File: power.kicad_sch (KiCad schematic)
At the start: 41 parts, among them U19 AP62301_TSOT, U20 AP62301_TSOT, U24 AP62301_TSOT, U38 TPS22976DPUR, U42 TPS22976DPUR

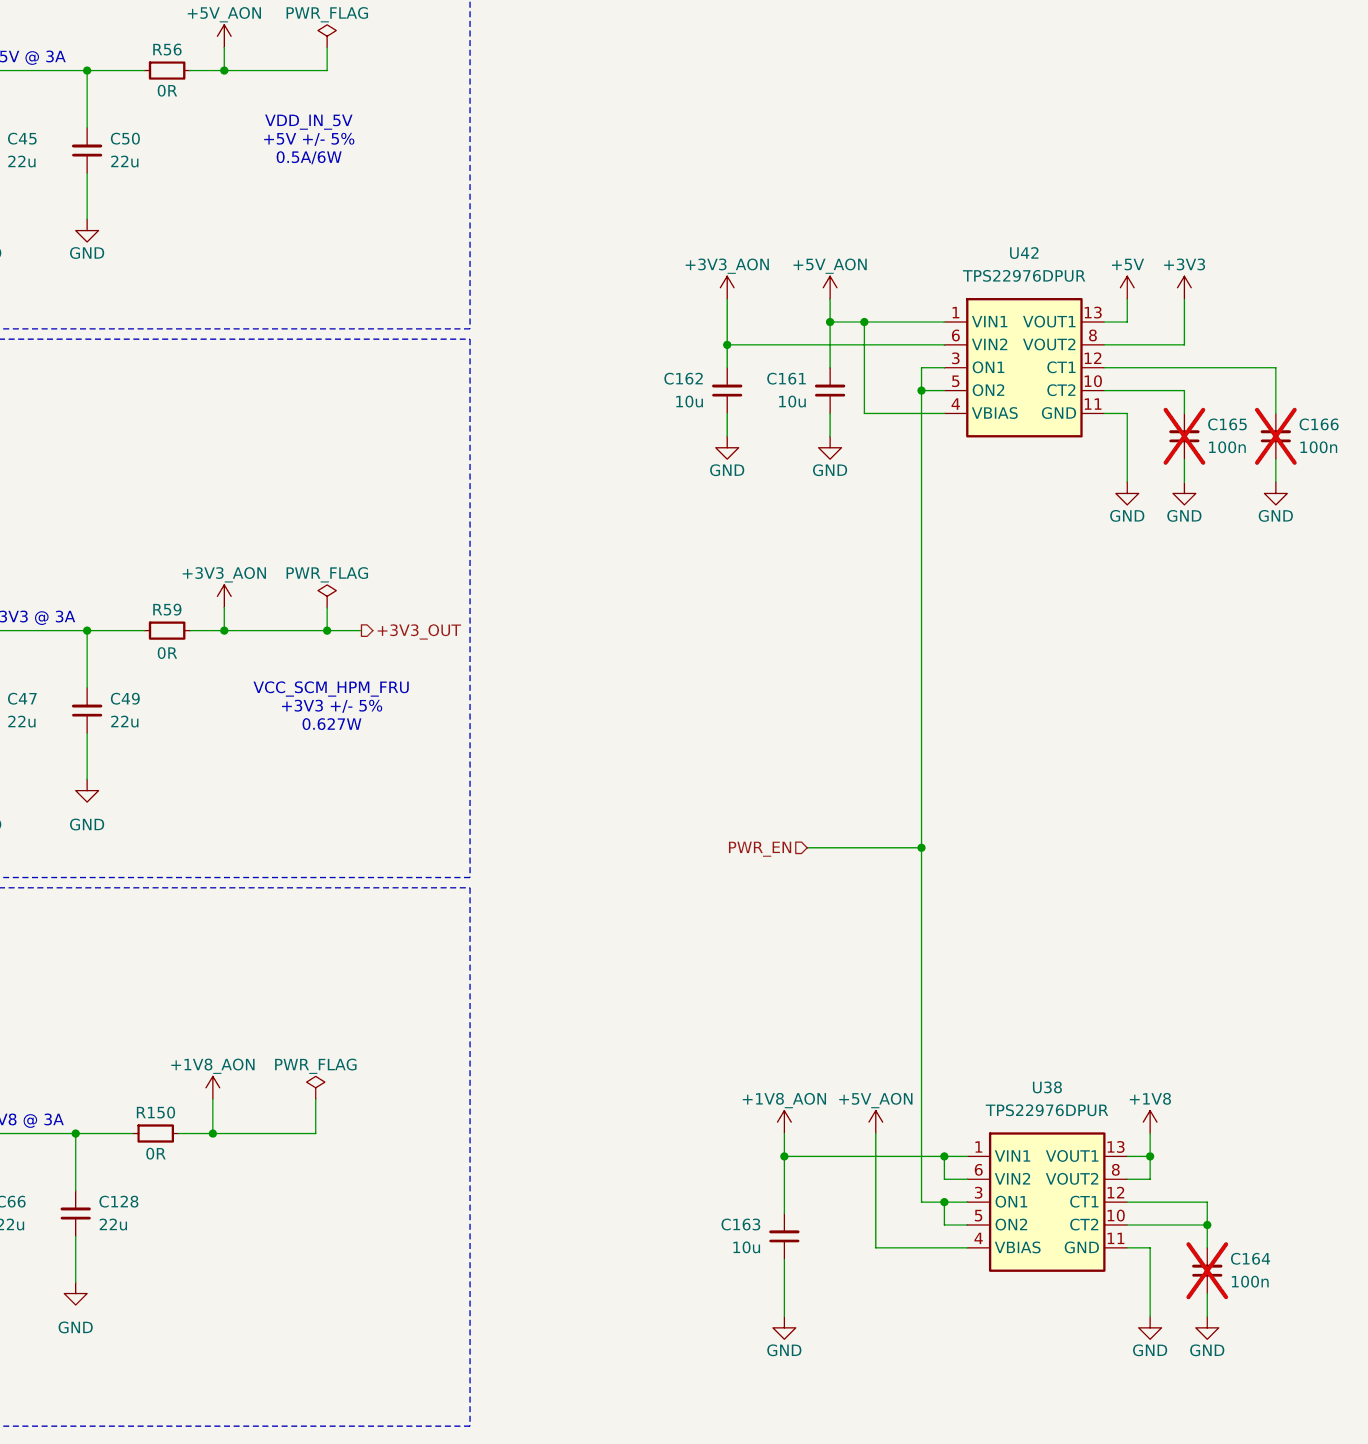
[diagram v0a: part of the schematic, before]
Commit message: [#83609] Connect PWR_EN signal, change eMMC power to AON, minor schematic refactor
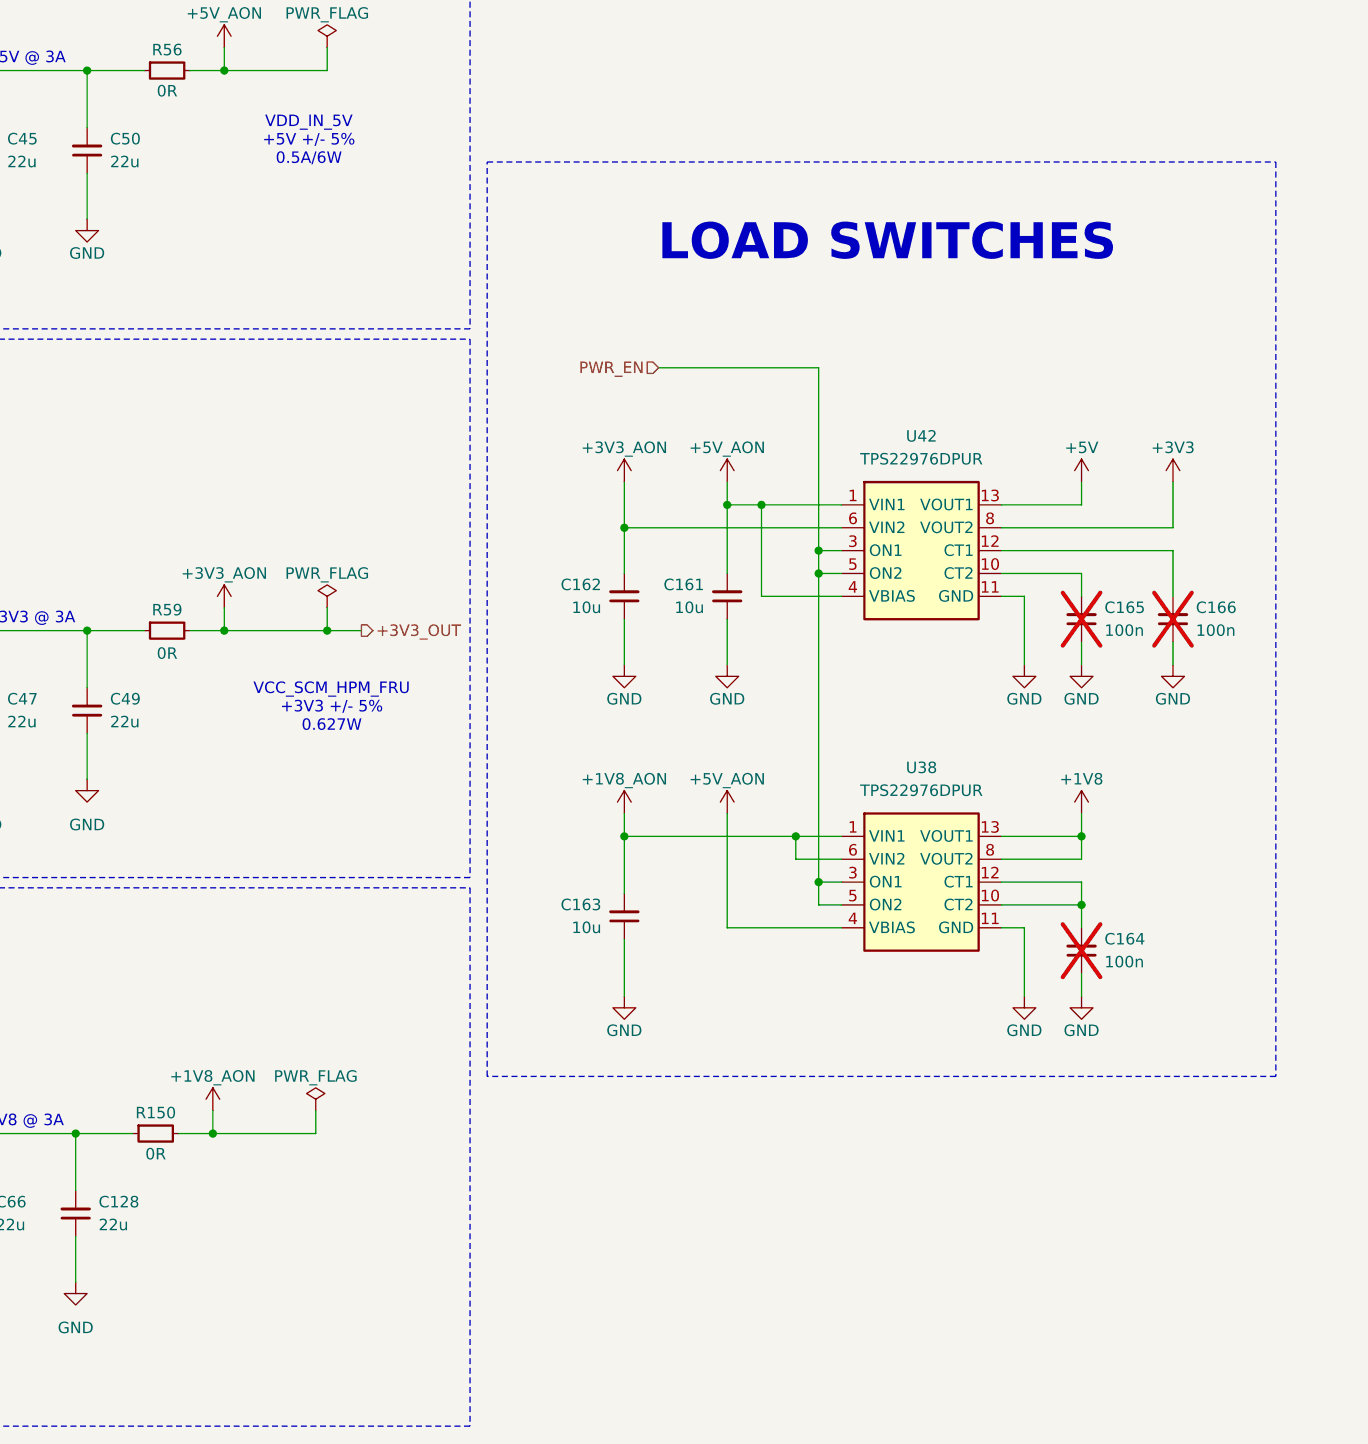
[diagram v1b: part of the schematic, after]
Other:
- note added: "LOAD SWITCHES"
- moved on the sheet: C161, C162, C163, C164, C165, C166, U38, U42

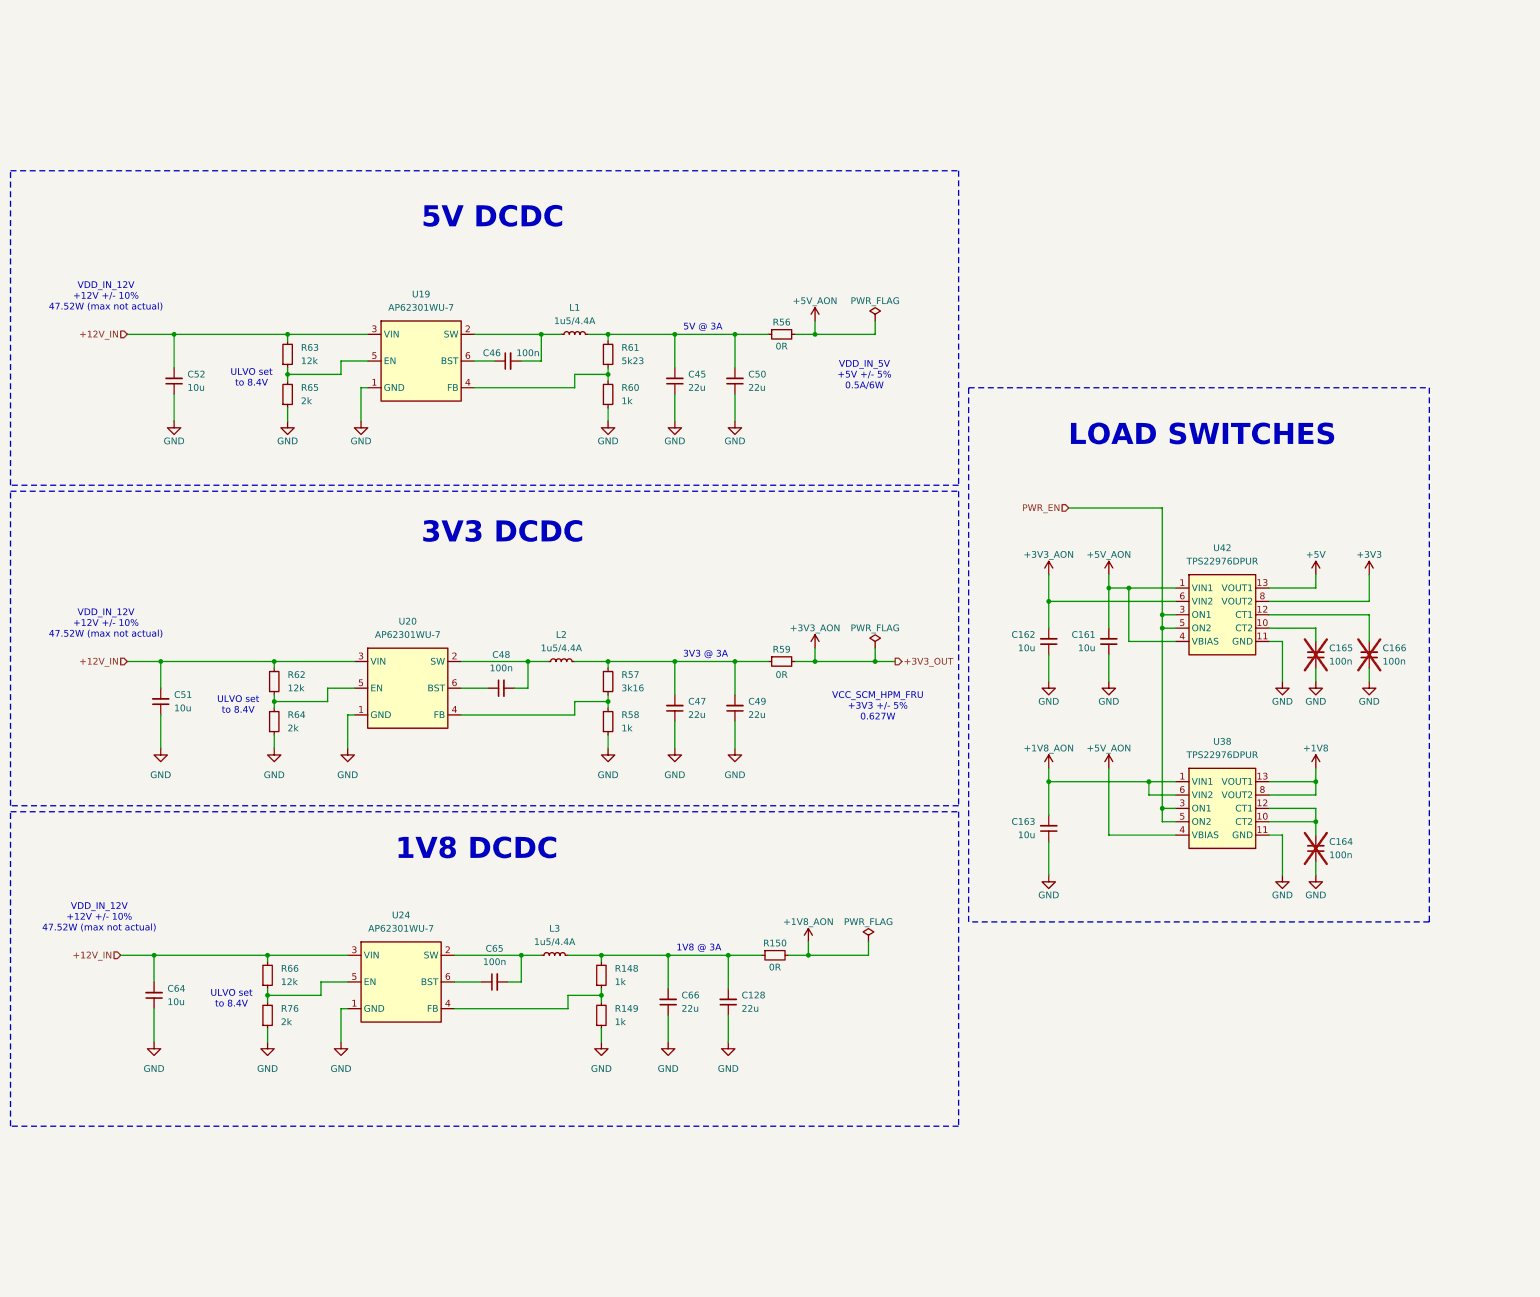
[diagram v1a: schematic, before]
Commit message: [#83609] Move +5V to double switch. Add indicator LEDs and TPs
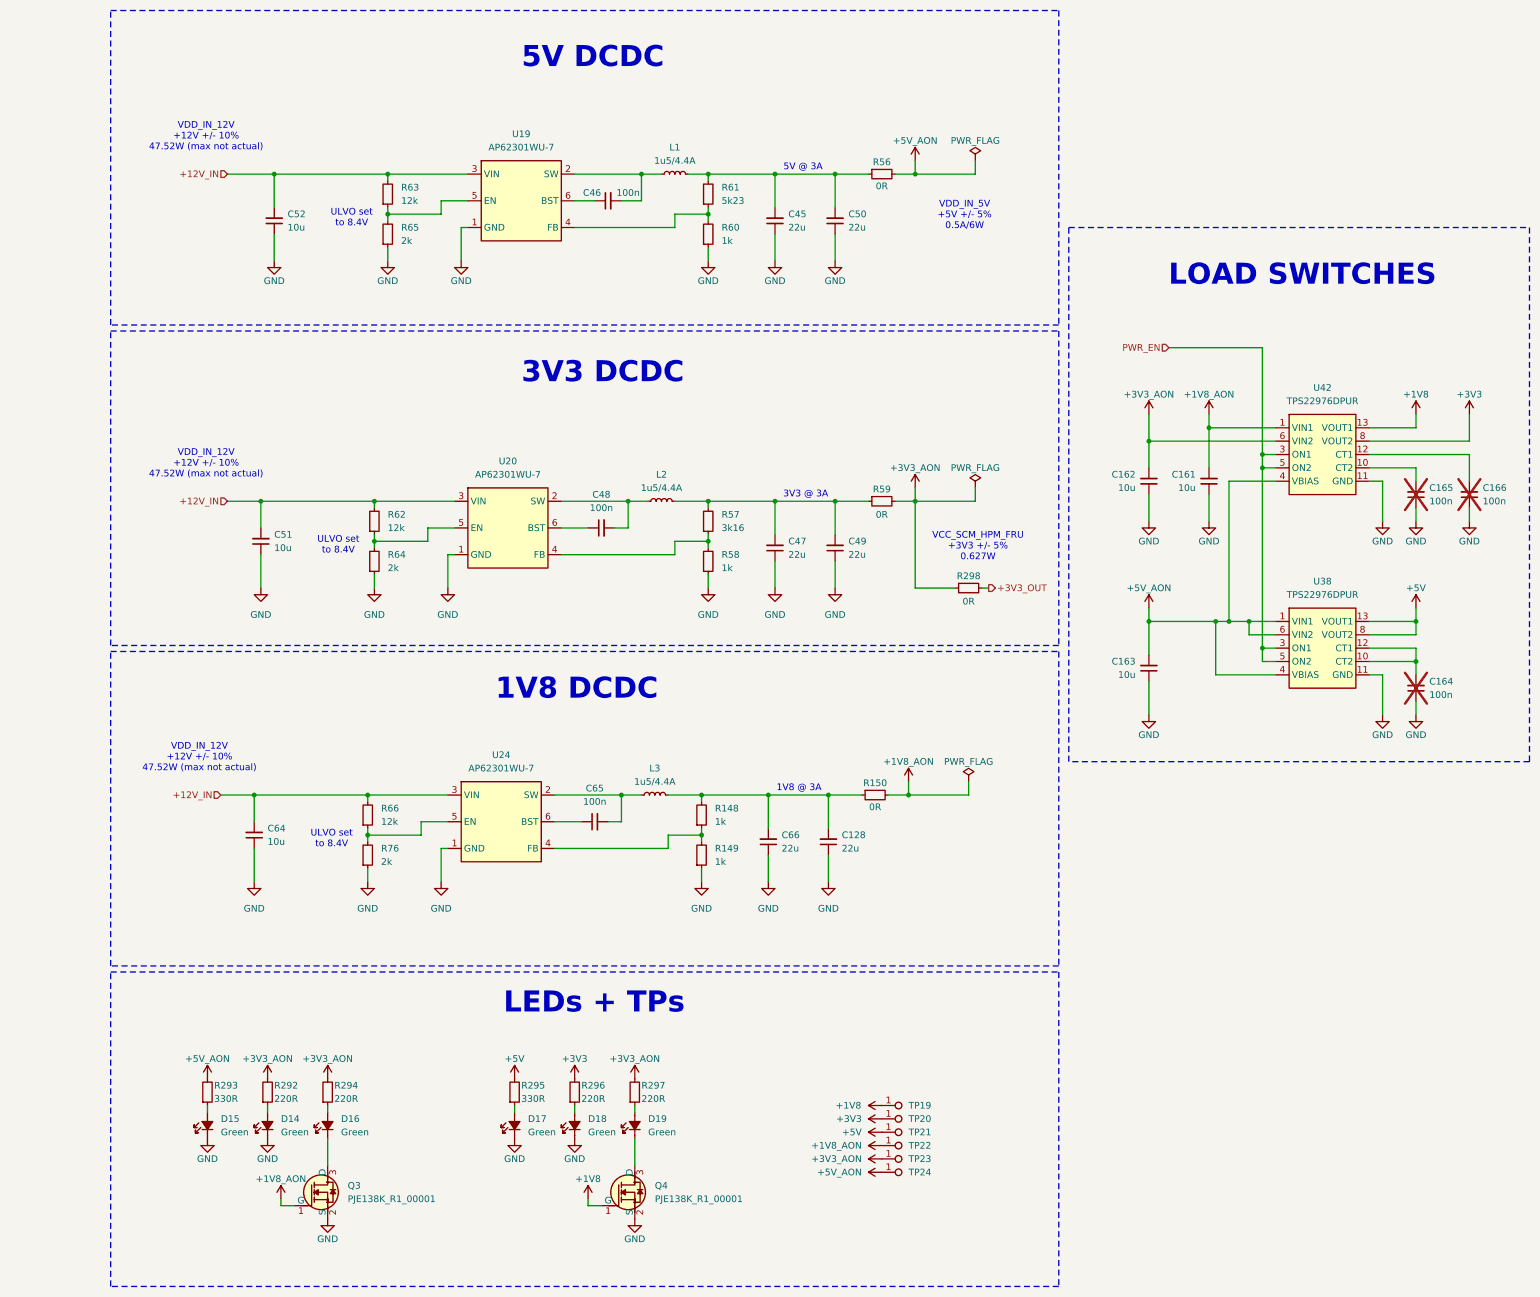
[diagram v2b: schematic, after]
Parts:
- added D14, D15, D16, D17, D18, D19: LED_G_0402_VLMTG1500-GS08, antmicro-footprints:LED_0402_1005Metric_G, symbol antmicroLEDIndicationDiscrete:LED_G_0402_VLMTG1500-GS08
- added Q3, Q4: PJE138K, antmicro-footprints:SOT-523, symbol antmicroTransistorsFETsMOSFETsSingle:PJE138K
- added R292, R294, R296, R297: R_220R_0402, antmicro-footprints:R_0402_1005Metric, symbol antmicroResistors0402:R_220R_0402
- added R293, R295: R_330R_0402, antmicro-footprints:R_0402_1005Metric, symbol antmicroResistors0402:R_330R_0402
- added R298: R_0R_0402, antmicro-footprints:R_0402_1005Metric, symbol antmicroResistors0402:R_0R_0402
- added TP19, TP20, TP21, TP22, TP23, TP24: TP_0.75mm_SMD, antmicro-footprints:TP_SMD_0.75mm, symbol antmicroTestPoints:TP_0.75mm_SMD
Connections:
- net +1V8: now also U42.13 (VOUT1), U42.14 (VOUT1), Q4.1 (G), TP19.1; no longer U38.13 (VOUT1), U38.14 (VOUT1), U38.8 (VOUT2), U38.9 (VOUT2)
- net +1V8_AON: now also C161.2, U42.1 (VIN1), U42.2 (VIN1), Q3.1 (G), TP22.1; no longer C163.2, U38.1 (VIN1), U38.2 (VIN1), U38.6 (VIN2), U38.7 (VIN2)
- net +3V3: now also R296.2, TP20.1
- net +3V3_AON: now also R292.2, R294.2, R297.2, R298.1, TP23.1
- net +5V: now also U38.13 (VOUT1), U38.14 (VOUT1), U38.8 (VOUT2), U38.9 (VOUT2), R295.2, TP21.1; no longer U42.13 (VOUT1), U42.14 (VOUT1)
- net +5V_AON: now also C163.2, U38.1 (VIN1), U38.2 (VIN1), U38.6 (VIN2), U38.7 (VIN2), R293.2, TP24.1; no longer C161.2, U42.1 (VIN1), U42.2 (VIN1)
- net GND: now also D14.1 (C), D15.1 (C), D17.1 (C), D18.1 (C), Q3.2 (S), Q4.2 (S)
- new net: D17.2 (A), R295.1
- new net: D15.2 (A), R293.1
- new net: D16.2 (A), R294.1
- new net: D18.2 (A), R296.1
- new net: D16.1 (C), Q3.3 (D)
- new net: D19.1 (C), Q4.3 (D)
- new net: D19.2 (A), R297.1
- new net: D14.2 (A), R292.1
- new net +3V3_OUT: R298.2
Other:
- note added: "LEDs + TPs"
- moved on the sheet: C128, C161, C162, C163, C164, C165, C166, C45, C46, C47, C48, C49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

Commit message: [#83609] Reannotate board
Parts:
- renumbered C64 to C133, C51 to C134, C52 to C135, C65 to C136, C48 to C137, C46 to C138, C66 to C139, C45 to C140, C47 to C141, C128 to C142, C50 to C143, C49 to C144, C162 to C145, C163 to C146, C161 to C147, C165 to C148, C164 to C149, C166 to C150, D15 to D13, D16 to D15, D17 to D16, D18 to D17, D19 to D18, L3 to L1, L1 to L3, Q3 to Q2, Q4 to Q3, R293 to R242, R292 to R243, R294 to R244, R66 to R245, R76 to R246, R62 to R247, R64 to R248, R63 to R249, R65 to R250, R295 to R251, R296 to R252, R297 to R253, R148 to R254, R149 to R255, R61 to R256, R60 to R257, R57 to R258, R58 to R259, R150 to R260, R56 to R261, R59 to R262, R298 to R263, TP19 to TP17, TP20 to TP18, TP21 to TP19, TP22 to TP20, TP23 to TP21, TP24 to TP22, U24 to U27, U20 to U28, U19 to U29, U42 to U30, U38 to U31

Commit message: [#83736] Change the 5V DC-DC conveter with more powerful one, refactor power schematic sheet
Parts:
- removed C135: C_10u_25V_0603, antmicro-footprints:C_0603_1608Metric, symbol antmicroCapacitors0603:C_10u_25V_0603
- removed C140, C143: C_22u_0805_16V, antmicro-footprints:C_0805_2012Metric, symbol antmicroCapacitorsmisc:C_22u_0805_16V
- removed L3: L_1u5_4.4A_Bourns-SRP3212A, antmicro-footprints:L_Bourns-SRP3212A, symbol antmicroFixedInductors:L_1u5_4.4A_Bourns-SRP3212A
- removed R249: R_12k_0402, antmicro-footprints:R_0402_1005Metric, symbol antmicroResistors0402:R_12k_0402
- removed R250: R_2k_0402, antmicro-footprints:R_0402_1005Metric, symbol antmicroResistors0402:R_2k_0402
- removed R256: R_5k23_0402, antmicro-footprints:R_0402_1005Metric, symbol antmicroResistors0402:R_5k23_0402
- removed R257: R_1k_0402, antmicro-footprints:R_0402_1005Metric, symbol antmicroResistors0402:R_1k_0402
- removed U29: AP62301_TSOT, antmicro-footprints:TSOT23-6, symbol antmicroDCDCConverters:AP62301_TSOT
- added C135, C140: C_100n_0402, antmicro-footprints:C_0402_1005Metric, symbol antmicroCapacitors0402:C_100n_0402
- added C143, C176: C_22u_25V_0805, antmicro-footprints:C_0805_2012Metric, symbol antmicroCapacitorsmisc:C_22u_25V_0805
- added C177, C178, C179, C180: C_22u_16V_0603, antmicro-footprints:C_0603_1608Metric_EIA, symbol antmicroCapacitors0603:C_22u_16V_0603
- added C181: C_1u_0402, antmicro-footprints:C_0402_1005Metric, symbol antmicroCapacitors0402:C_1u_0402
- added C182: C_4u7_25V_0402, antmicro-footprints:C_0402_1005Metric, symbol antmicroCapacitors0402:C_4u7_25V_0402
- added L4: L_1u_20A_Bourns-SRP6050CA, antmicro-footprints:L_Bourns-SRP6050CA, symbol antmicroFixedInductors:L_1u_20A_Bourns-SRP6050CA
- added R249: R_20k_0402, antmicro-footprints:R_0402_1005Metric, symbol antmicroResistors0402:R_20k_0402
- added R250: R_2k7_0402, antmicro-footprints:R_0402_1005Metric, symbol antmicroResistors0402:R_2k7_0402
- added R256, R342, R343: R_499k_0402, antmicro-footprints:R_0402_1005Metric, symbol antmicroResistors0402:R_499k_0402
- added R257: R_73k2_0402, antmicro-footprints:R_0402_1005Metric, symbol antmicroResistors0402:R_73k2_0402
- added R341: R_10k_0402, antmicro-footprints:R_0402_1005Metric, symbol antmicroResistors0402:R_10k_0402
- added U29: SIC431AED-T1-GE3, antmicro-footprints:MLP44-24L_4x4x0.75mm, symbol antmicroDCDCConverters:SIC431AED-T1-GE3
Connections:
- net +12V_IN: now also C140.1, C143.2, C176.2, U29.1 (V_{IN}), U29.2 (V_{IN}), U29.22 (V_{IN}), U29.26 (V_{IN})
- net GND: now also C135.2, C140.2, C143.1, C176.1, C177.1, C178.1, C179.1, C180.1, C181.1, C182.1, R250.1, R341.1, R342.1, R343.1, U29.13 (P_{GND}), U29.16 (A_{GND}), U29.25 (A_{GND}), U29.27 (P_{GND}), U29.3 (P_{GND}), U29.4 (P_{GND})
- net 5V_OUT: now reaches R261.1
- net 5V_OUT: now also C177.2, C178.2, C179.2, C180.2, L4.2, R257.2, U29.18 (V_{OUT})
- net 5V_BOOT: now reaches C138.2
- net 5V_BOOT: now also U29.23 (BOOT)
- net 5V_PHASE: now reaches C138.1
- net 5V_PHASE: now also U29.24 (PHASE)
- net 1V8_OUT: now reaches C139.2, C142.2, L1.2, R254.2, R260.1
- net 3V3_OUT: now reaches C141.2, C144.2, L2.2, R258.2, R262.1
- new net: U29.10 (GL), U29.11 (GL), U29.28 (GL)
- new net 5V_EN: C135.1, R249.1, R250.2, U29.19 (EN)
- new net 5V_FB: R257.1, R341.2, U29.17 (FB)
- new net 5V_MODE1: R256.1, R342.2, U29.21 (MODE1)
- new net 5V_MODE2: R343.2, U29.20 (MODE2)
- new net 5V_SW: L4.1, U29.5 (SW), U29.6 (SW), U29.7 (SW), U29.8 (SW), U29.9 (SW)
- new net 5V_VDD: C181.2, R256.2, U29.15 (V_{DD})
- new net 5V_VDRV: C182.2, U29.12 (V_{DRV})
- new net VCC: R249.2
- no-connect marks 0 -> 2
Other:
- note added: "5V @ 12A"
- note added: "R_{FB_H} = (R_{FB_L}(V_{OUT}-0.6))/0.6"
- note added: "V_{OUT} = 0.6*(73k2+10k)/10k = 4.992[V]"
- note added: "V_{OUT} = 0.6*(R_{FB_H}+R_{FB_L})/R_{FB_L}"
- note removed: "5V @ 3A"
- moved on the sheet: C133, C134, C136, C137, C139, C141, C142, C144, C145, C146, C147, C148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
